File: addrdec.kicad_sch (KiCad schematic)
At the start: 5 parts, among them U10 74LS138, U11 74HCT00, U5 74HCT02, U8 74LS04, U9 74LS27

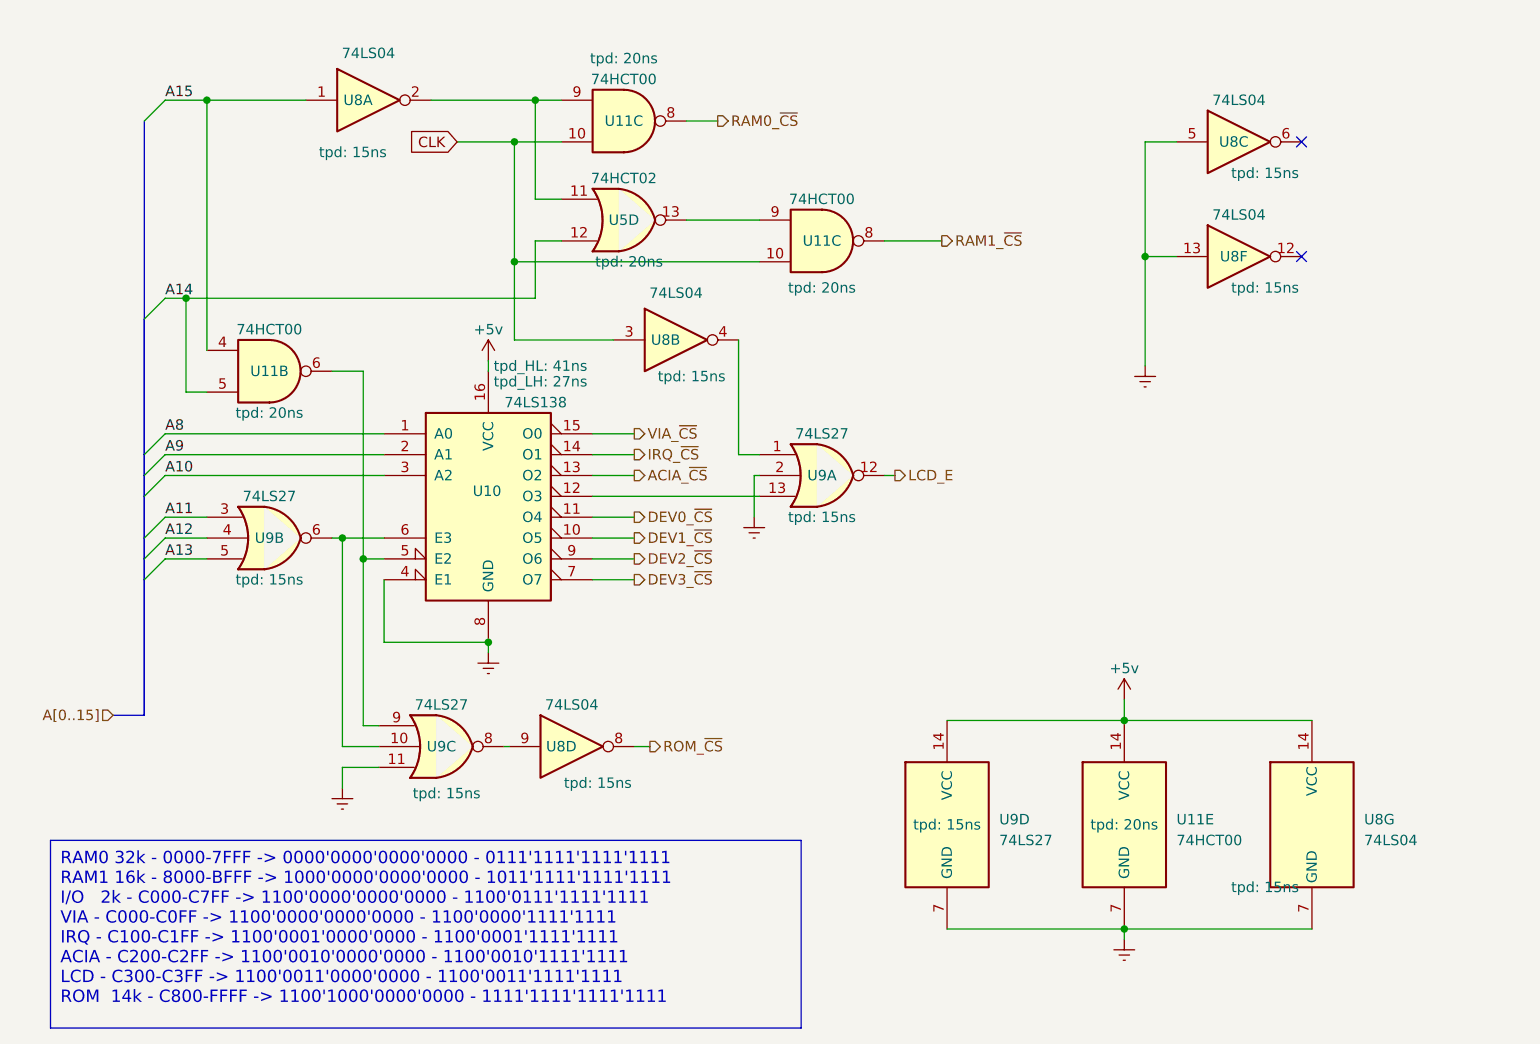
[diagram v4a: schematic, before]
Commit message: RS-232/ACIA works!
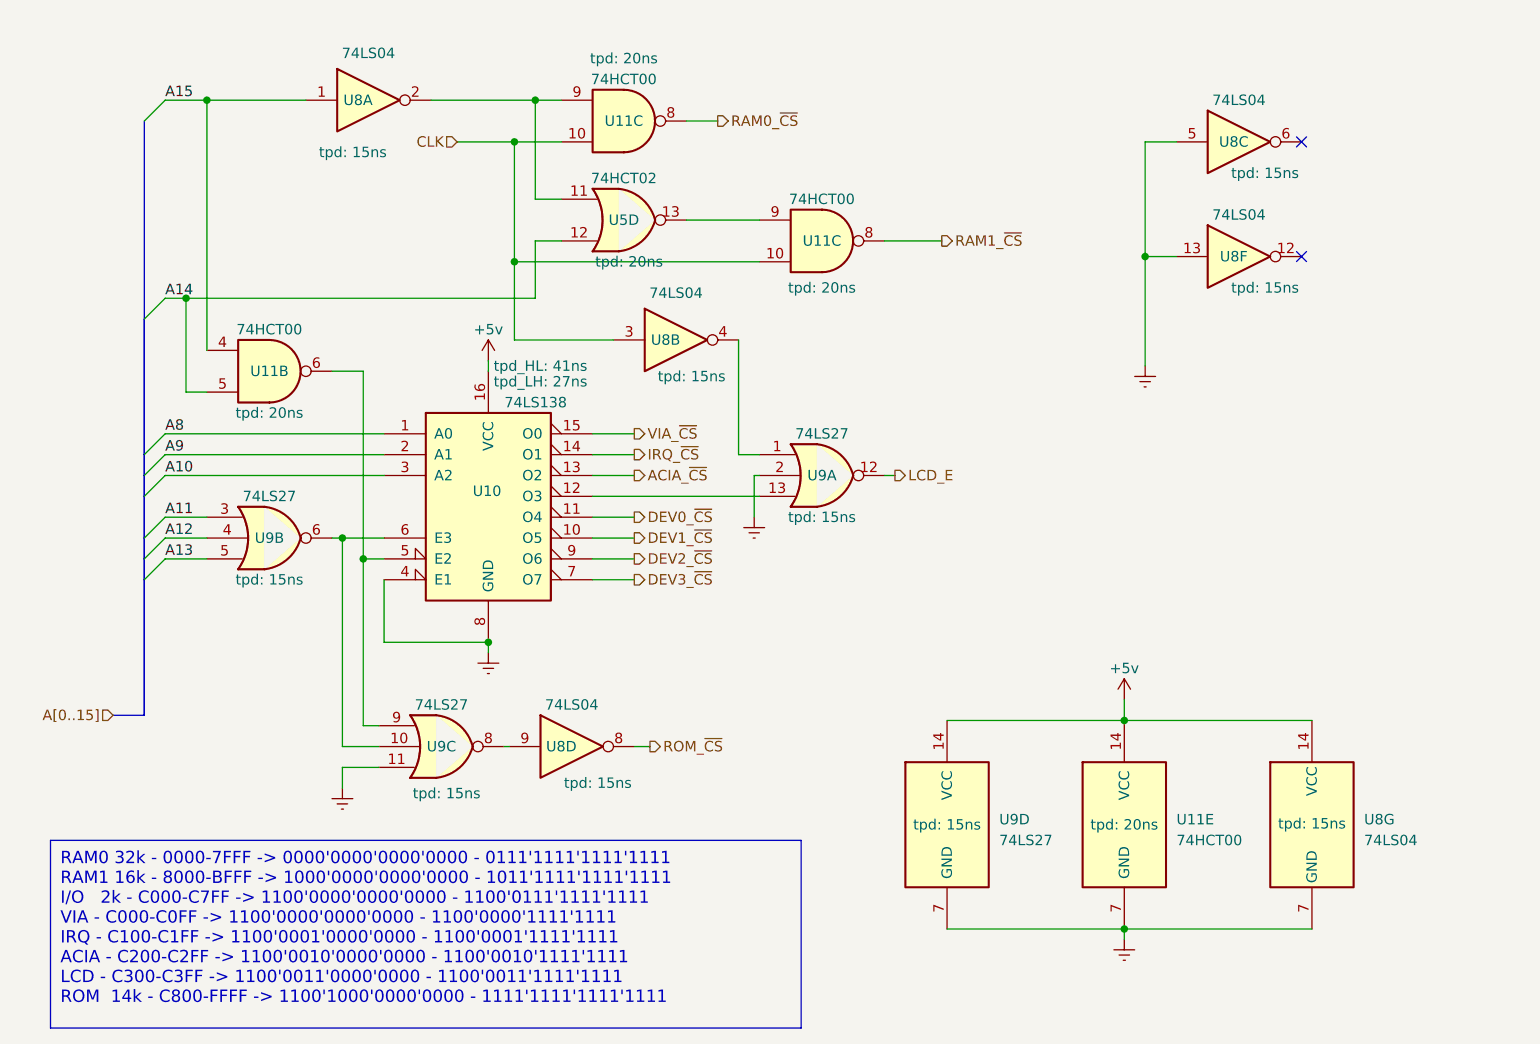
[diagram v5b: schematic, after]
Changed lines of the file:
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@@
     (effects (font (size 1.27 1.27)) (justify left bottom))
-  )
-  (global_label "CLK" (shape input) (at 66.04 29.21 180) (fields_autoplaced)
-    (effects (font (size 1.27 1.27)) (justify right))
-    (property "Intersheetrefs" "${INTERSHEET_REFS}" (at 59.5661 29.21 0)
-      (effects (font (size 1.27 1.27)) (justify right) hide)
-    )
   )
   (hierarchical_label "ACIA_~{CS}" (shape output) (at 87.63 69.85 0) (fields_autoplaced)
@@
   (hierarchical_label "DEV0_~{CS}" (shape output) (at 87.63 74.93 0) (fields_autoplaced)
     (effects (font (size 1.27 1.27)) (justify left))
+  )
+  (hierarchical_label "CLK" (shape input) (at 66.04 29.21 180) (fields_autoplaced)
+    (effects (font (size 1.27 1.27)) (justify right))
   )
   (hierarchical_label "ROM_~{CS}" (shape output) (at 89.535 102.87 0)
@@
   )
   (symbol (lib_id "74xx:74LS04") (at 170.18 112.395 0) (unit 7)
-    (in_bom yes) (on_board yes) (dnp no) (fields_autoplaced)
+    (in_bom yes) (on_board yes) (dnp no)
     (property "Reference" "U8" (at 176.53 111.76 0)
       (effects (font (size 1.27 1.27)) (justify left))
@@
       (effects (font (size 1.27 1.27)) hide)
     )
-    (property "tpd" "15ns" (at 164.465 120.015 0) (show_name)
-      (effects (font (size 1.27 1.27)))
-    )
+    (property "tpd" "15ns" (at 170.18 112.268 0) (show_name)
+      (effects (font (size 1.27 1.27)))
+    )

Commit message: adjust timings to fast IC for address decoding
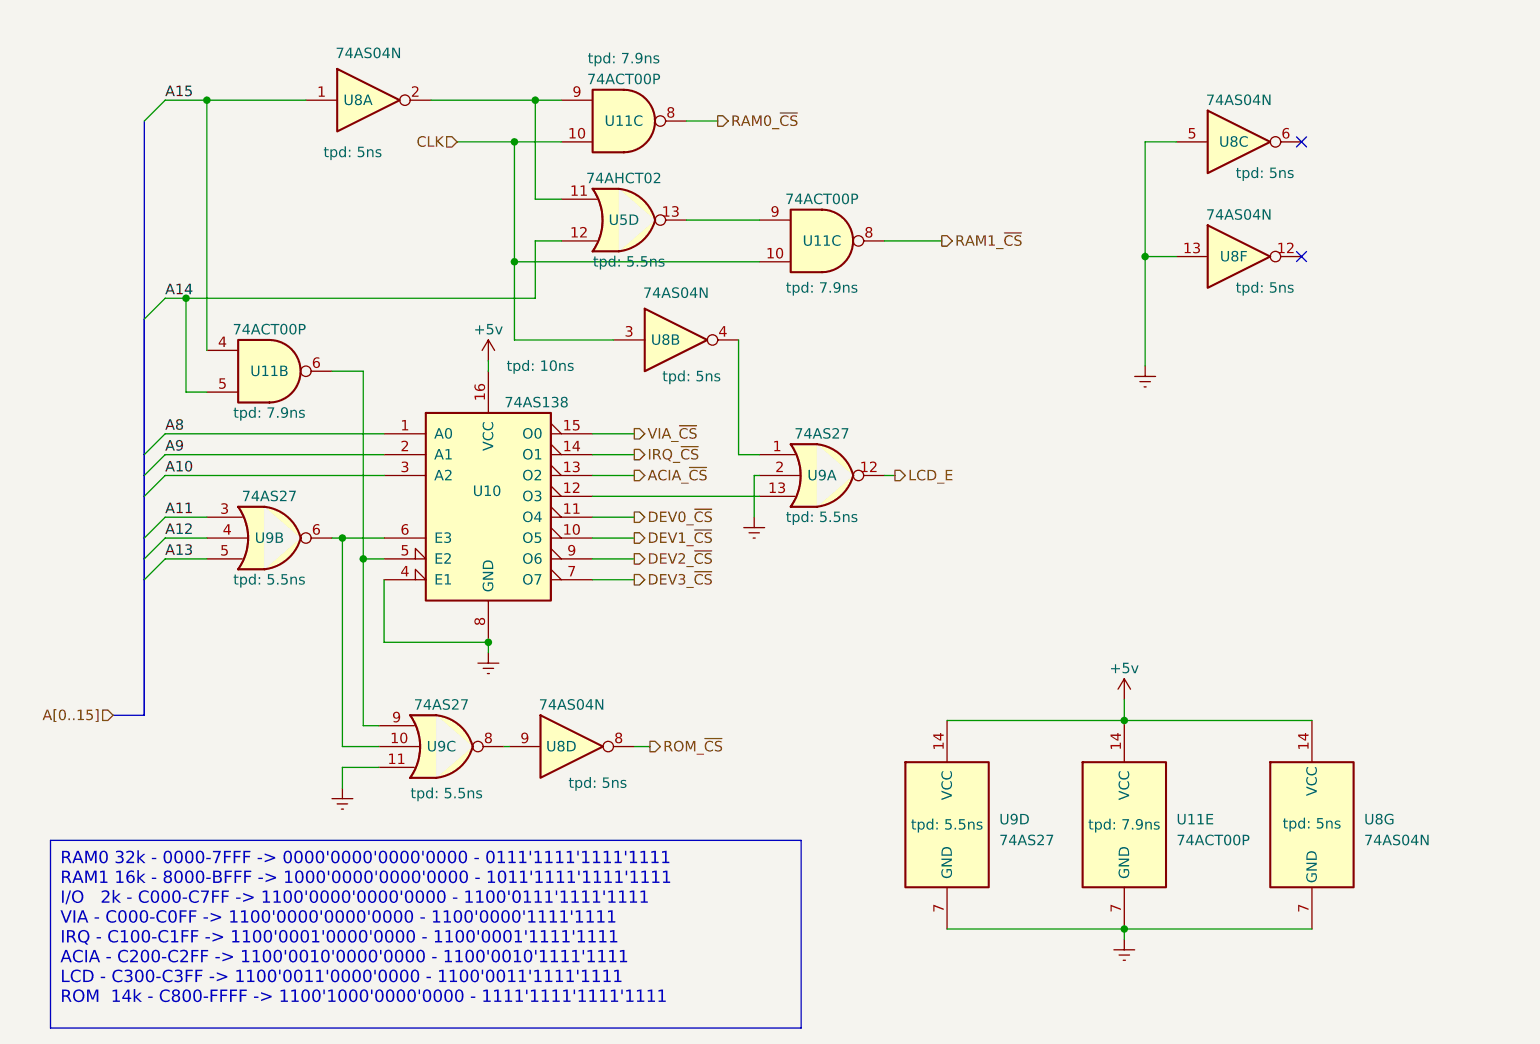
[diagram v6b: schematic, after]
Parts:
- U10: value 74LS138 -> 74AS138; tpd (none) -> 10ns; tpd_HL 41ns -> (none); tpd_LH 27ns -> (none)
- U11: value 74HCT00 -> 74ACT00P; tpd 20ns -> 7.9ns
- U5: value 74HCT02 -> 74AHCT02; tpd 20ns -> 5.5ns
- U8: value 74LS04 -> 74AS04N; tpd 15ns -> 5ns
- U9: value 74LS27 -> 74AS27; tpd 15ns -> 5.5ns
